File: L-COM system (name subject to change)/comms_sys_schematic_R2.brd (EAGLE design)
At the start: 43 x 72 mm, 45 parts, among them U1 TLV75733PDBVR, Y1 ECS-TXO-2016-33-120-TR

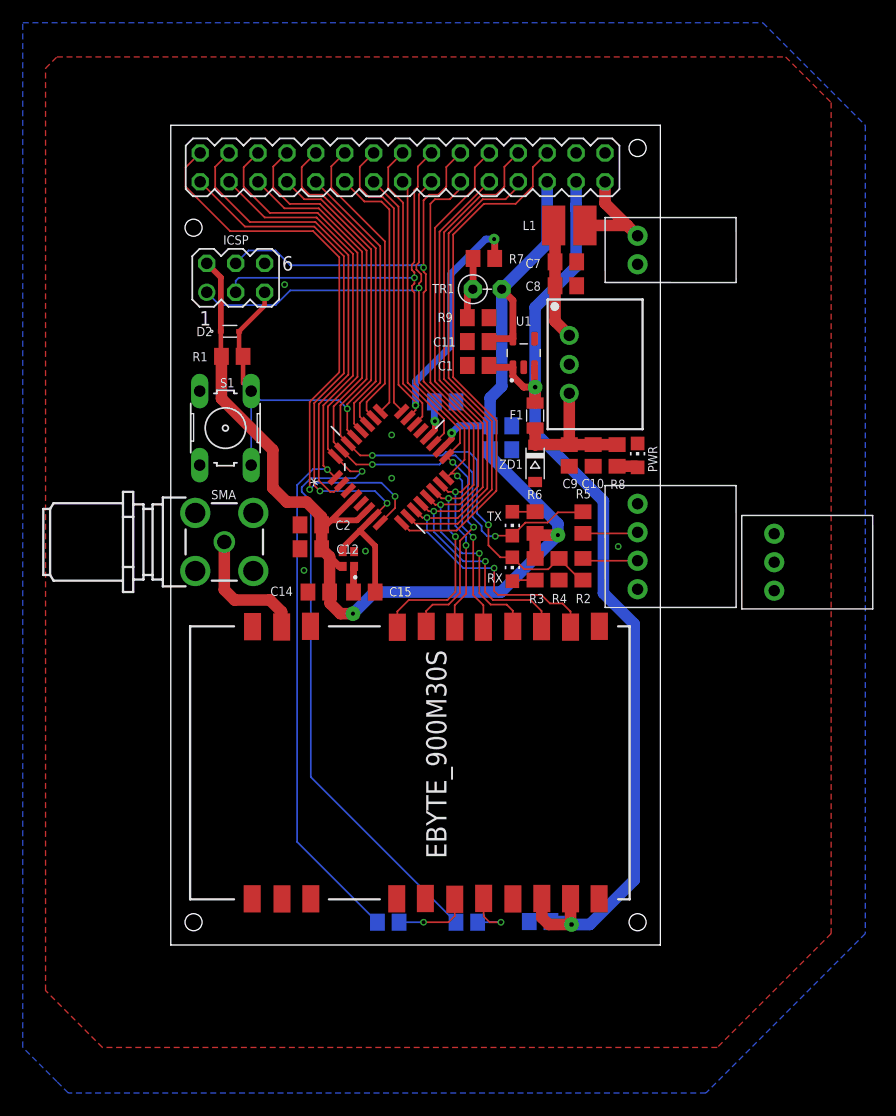
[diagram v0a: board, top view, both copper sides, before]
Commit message: Touch-ups to board
Small changes to the board, namely ensuring the antenna trace is properly designed (40 mil width for antenna-matching 50-Ohm impedance, via fence, removal of thermal reliefs on SMA connector).
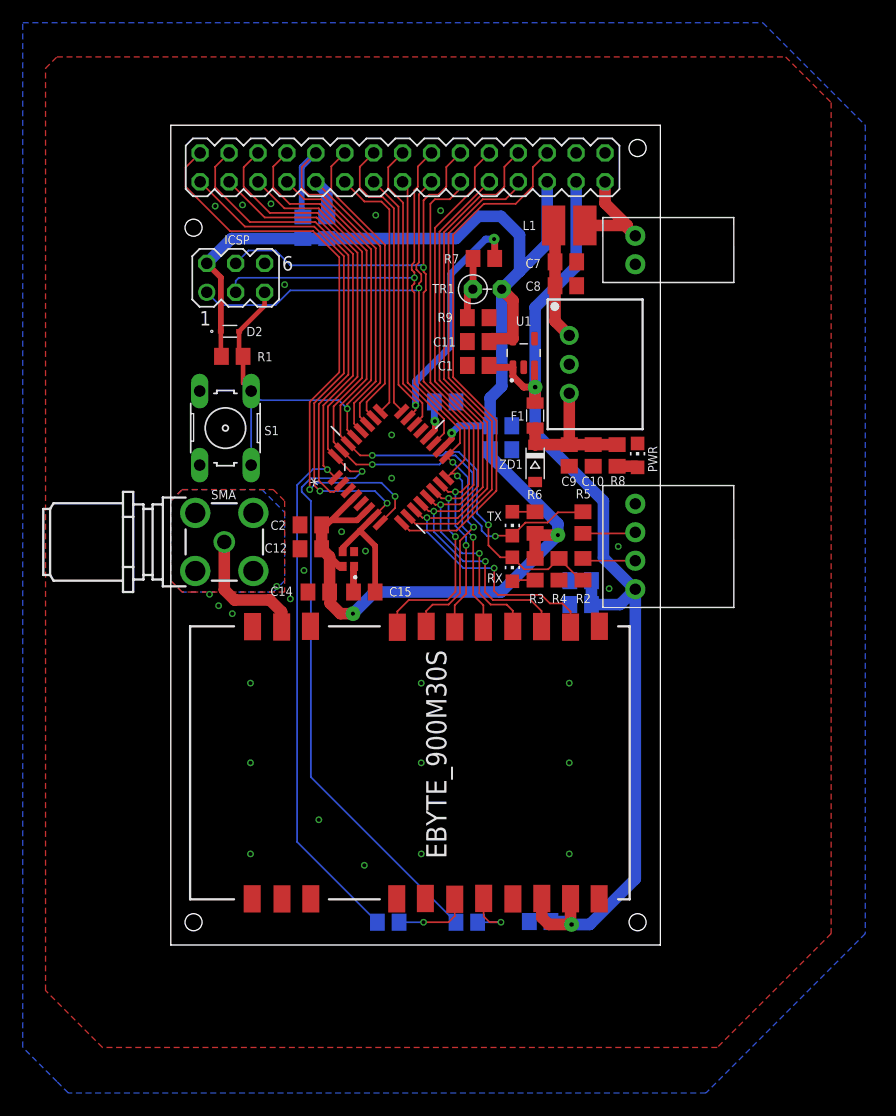
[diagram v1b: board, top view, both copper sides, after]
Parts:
- removed U$1: MINI-LOCK_3, cust_parts:MINI-LOCK_3
- added C5: 0.1uF, rcl:C0805
- added C6: 10uF, rcl:C0805
- added R12, R13: 4K7, rcl:R0805
- moved U$2 0.20 mm to (40.8, 61.0)
- moved U$3 0.20 mm to (40.8, 35.0)
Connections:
- net +3.3V: now also R12.1, R13.1
- net +5V: now also C5.2, C6.2, U$3.+5V
- net GND: now also C5.1, C6.1
- net PC4: now also R12.2
- net PC5: now also R13.2
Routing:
- net +3.3V: track 120.0 -> 133.6 mm
- net +5V: track 90.8 -> 97.4 mm
- net PC5: track 29.3 -> 35.5 mm
- net PC4: track 24.7 -> 28.1 mm
- net PD0: track 62.6 -> 62.1 mm
